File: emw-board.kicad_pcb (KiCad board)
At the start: 2 copper layers, 49.5 x 48.3 mm, 36 parts, among them P1 1WIRE, P2 BATT, P3 CONN_01X06, P4 SWDN, P5 CONS, P6 OLED, P7 CONN_01X07, SW1 B3S-1000, SW2 B3S-1000, U1 MAX604CSA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

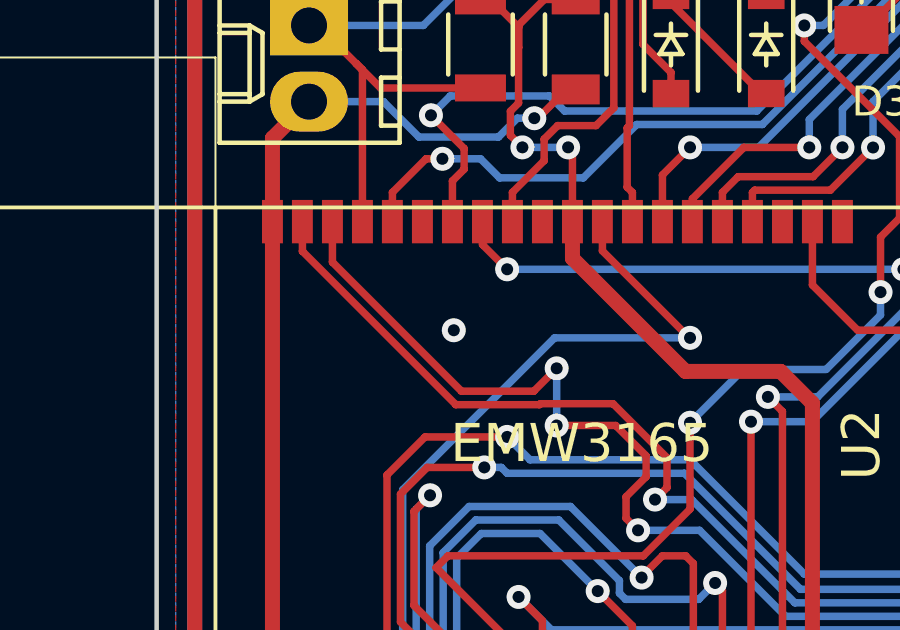
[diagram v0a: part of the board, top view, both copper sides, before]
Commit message: Regenerate copper pours.
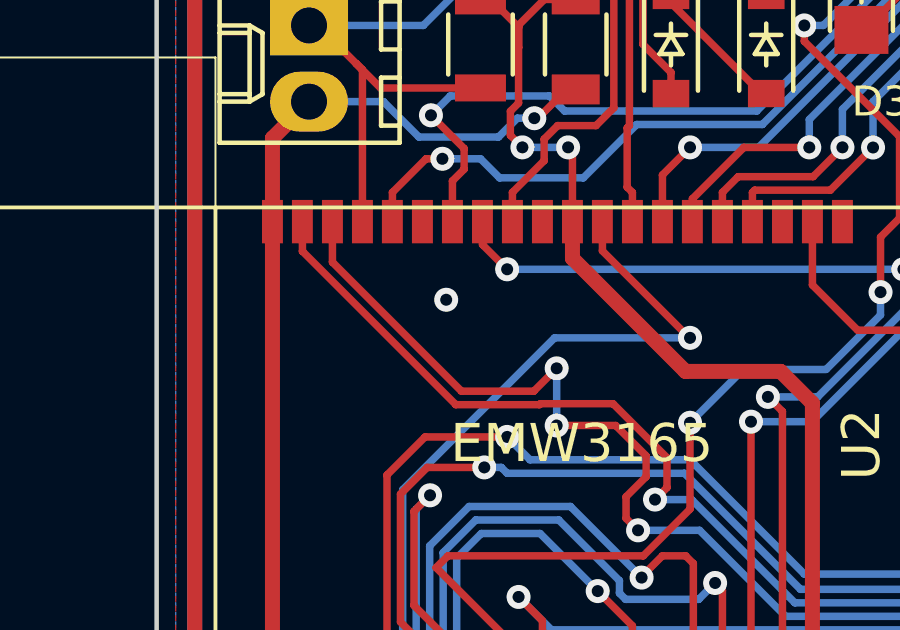
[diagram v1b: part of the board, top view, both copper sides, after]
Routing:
- net GND: vias 7 -> 8
- net (no net): vias 1 -> 0
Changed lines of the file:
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@@
     (visible_elements 7FFEFF7F)
     (pcbplotparams
-      (layerselection 0x010f0_ffffffff)
+      (layerselection 0x010f0_80000001)
       (usegerberextensions true)
       (excludeedgelayer true)
@@
   (gr_line (start 163.83 53.34) (end 163.83 101.6) (layer Edge.Cuts) (width 0.15))
   (gr_line (start 114.3 53.34) (end 163.83 53.34) (layer Edge.Cuts) (width 0.15))
-  (via (at 124.206 72.39) (size 0.8) (drill 0.4) (layers F.Cu B.Cu) (net 0))
   (segment (start 119.38 62.23) (end 123.19 62.23) (width 0.25) (layer B.Cu) (net 1) (status 10))
   (segment (start 123.19 62.23) (end 125.73 59.69) (width 0.25) (layer B.Cu) (net 1))
@@
   (segment (start 123.31841 76.962) (end 125.222 76.962) (width 0.25) (layer F.Cu) (net 4))
   (via (at 125.222 76.962) (size 0.8) (drill 0.4) (layers F.Cu B.Cu) (net 4))
+  (via (at 123.952 71.374) (size 0.8) (drill 0.4) (layers F.Cu B.Cu) (net 8))
   (segment (start 159.512 88.392) (end 159.512 89.892) (width 0.5) (layer F.Cu) (net 8) (status 10))
   (segment (start 159.512 89.892) (end 157.48 91.924) (width 0.5) (layer F.Cu) (net 8))

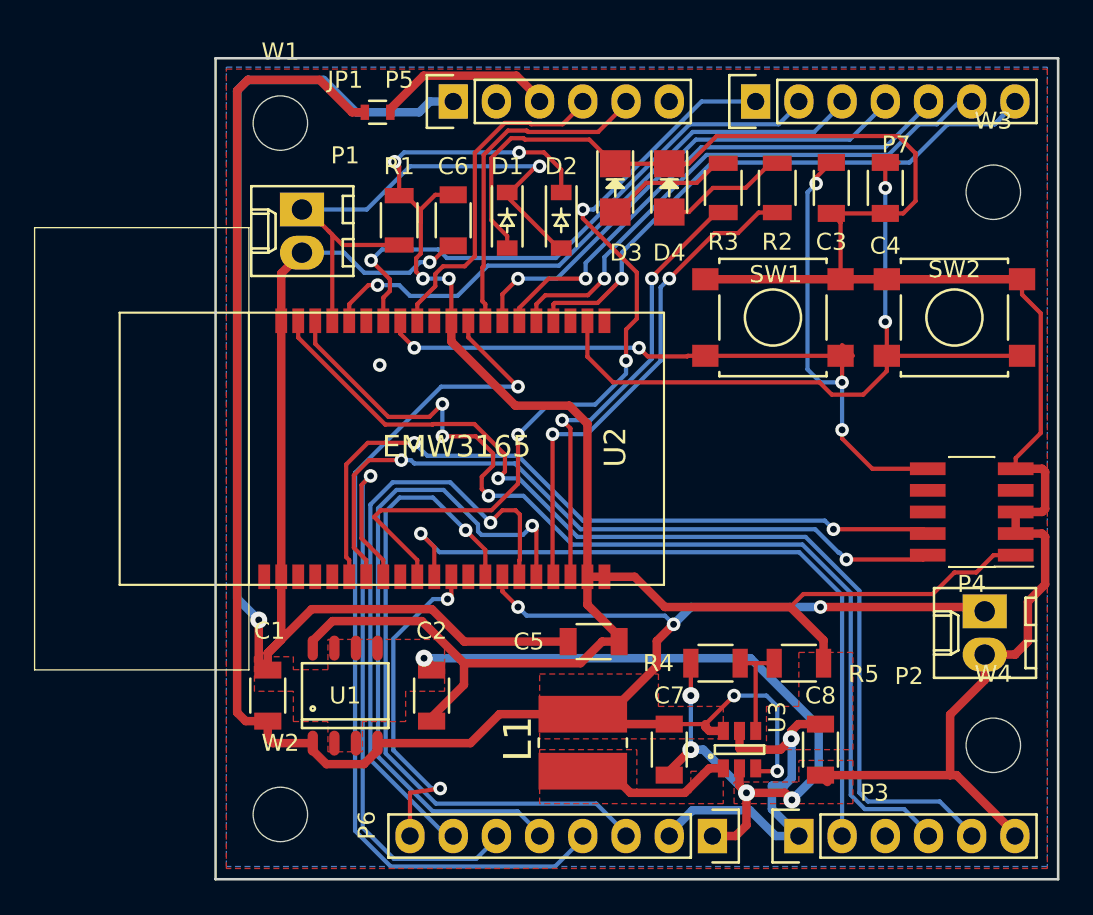
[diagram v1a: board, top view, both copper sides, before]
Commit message: Move power and 1-wire connector so that right-angled type can also be used.
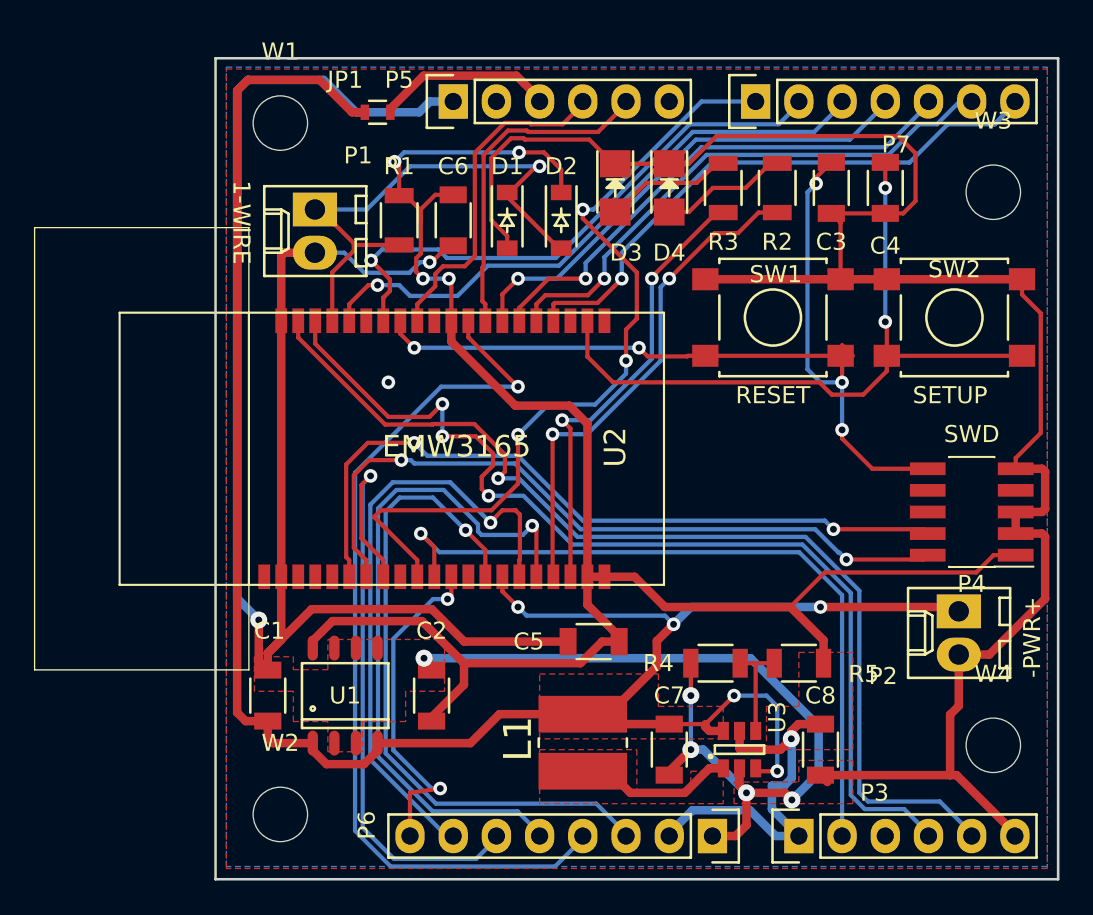
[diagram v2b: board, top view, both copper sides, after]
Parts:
- moved P2 1.52 mm to (158.0, 85.9)
- moved P1 0.76 mm to (120.1, 62.2)
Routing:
- net +BATT: track 127.6 -> 125.5 mm
- net Net-(D1-Pad1): track 34.2 -> 33.1 mm
- net GND: track 270.9 -> 271.5 mm
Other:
- board text added: "-PWR+"
- board text added: "1-WIRE"
- board text added: "RESET"
- board text added: "SETUP"

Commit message: Rotate 1-wire connector.
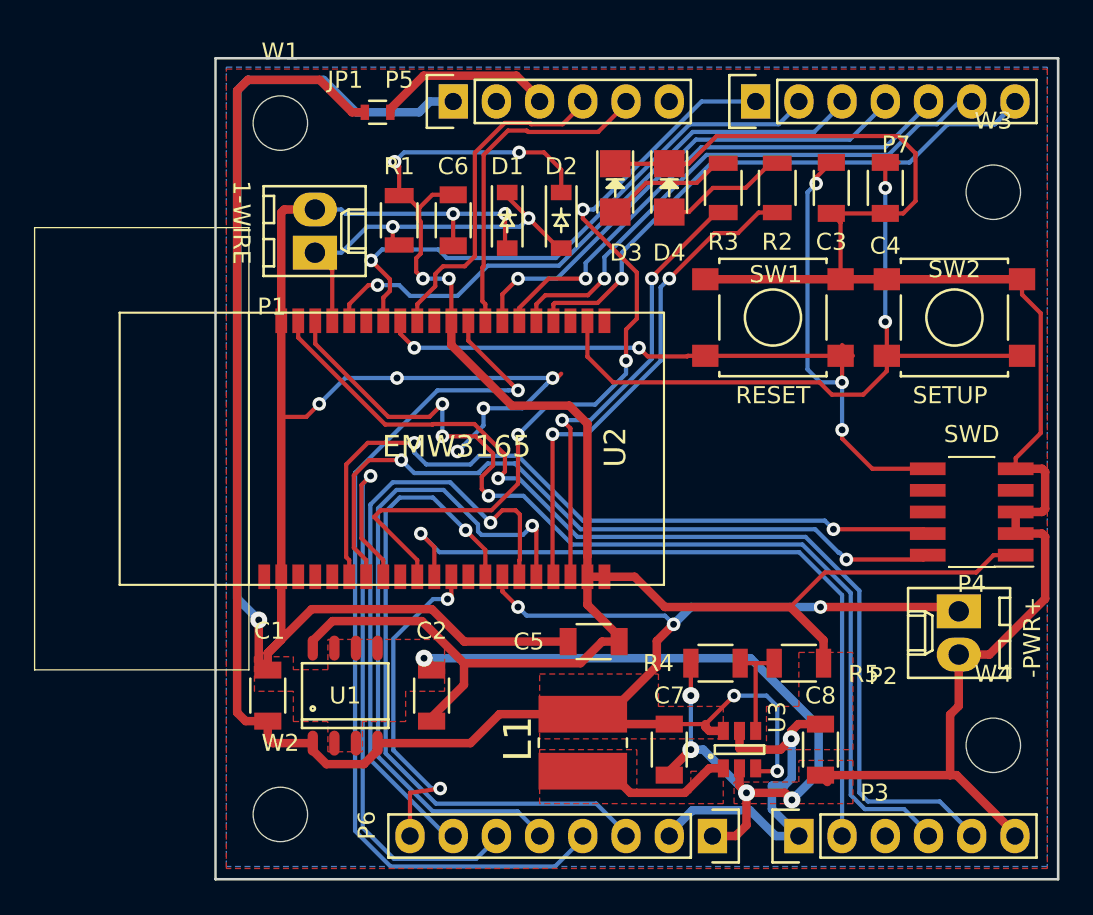
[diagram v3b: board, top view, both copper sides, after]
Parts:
- moved P1 2.54 mm to (120.1, 64.8), turned to 90 degrees
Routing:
- net GND: track 271.5 -> 291.8 mm, vias 8 -> 13
- net Net-(D1-Pad1): track 33.1 -> 24.2 mm, vias 1 -> 2
- net Net-(P4-Pad4): track 43.6 -> 44.4 mm
- net Net-(P4-Pad2): track 42.9 -> 43.4 mm

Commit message: Fix swd connector placing.
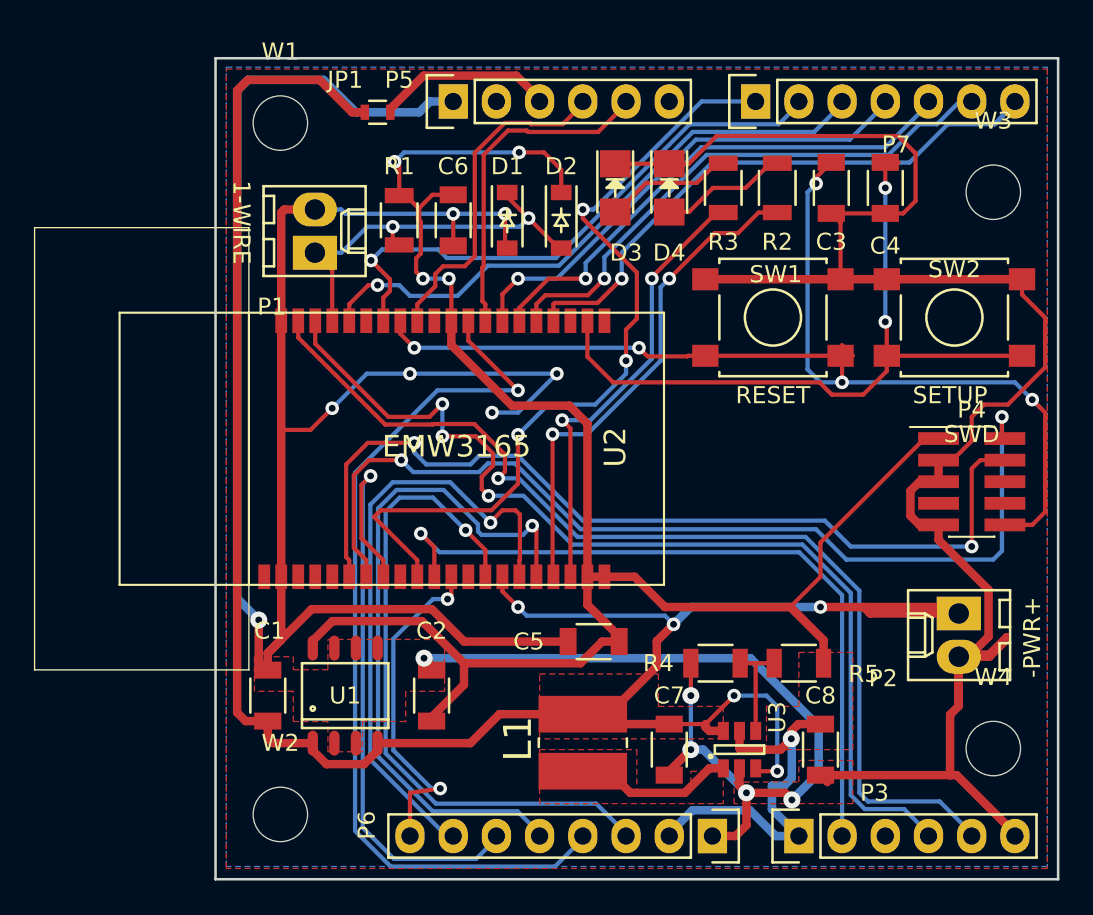
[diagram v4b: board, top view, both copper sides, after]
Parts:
- P4: footprint Pin_Headers:Pin_Header_Straight_2x05_Pitch1.27mm_SMD -> stonepile:swd_connector_2x05_Pitch1.27mm_SMD
- moved P4 1.78 mm to (158.8, 78.2), turned to 0 degrees
- moved W4 0.19 mm to (160.0, 93.9)
- moved P2 0.13 mm to (158.0, 86.0)
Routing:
- net Net-(P4-Pad2): track 43.4 -> 57.0 mm
- net Net-(C3-Pad1): track 54.6 -> 68.1 mm
- net Net-(P4-Pad4): track 44.4 -> 54.0 mm
- net GND: track 291.8 -> 298.6 mm, vias 13 -> 12
- net +BATT: track 125.5 -> 131.3 mm
- net +3V3: track 131.3 -> 130.7 mm

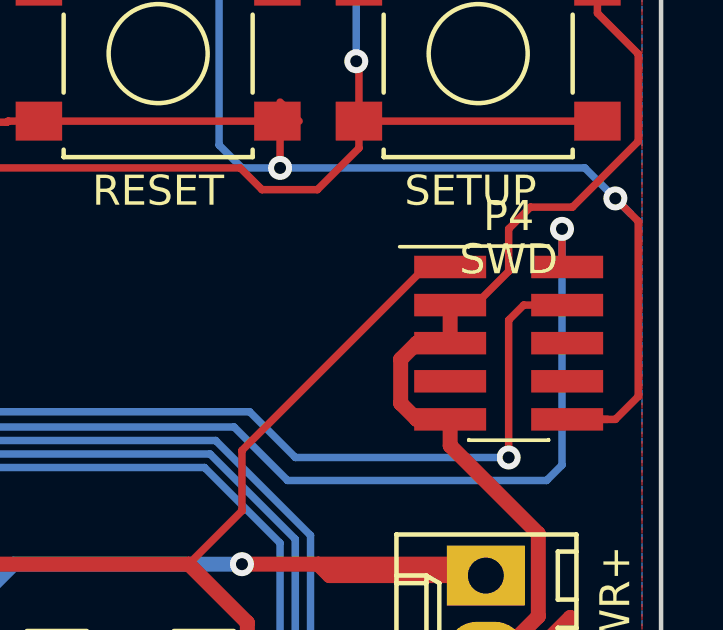
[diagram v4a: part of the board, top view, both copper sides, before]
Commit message: Add BOM info.
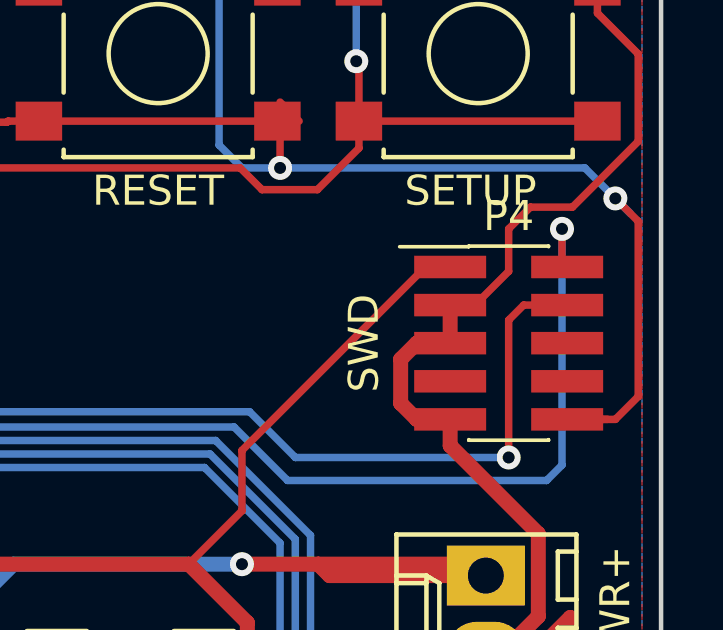
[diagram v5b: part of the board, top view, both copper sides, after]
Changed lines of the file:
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@@
     (links 93)
     (no_connects 0)
-    (area 114.224999 53.264999 163.905001 101.675001)
+    (area 103.429459 50.846666 163.905001 104.093333)
     (thickness 1.6)
     (drawings 38)
@@
     (effects (font (size 1.5 1.5) (thickness 0.3)) (justify mirror))
   )
-  (gr_text SWD (at 158.75 75.438) (layer F.SilkS)
+  (gr_text SWD (at 153.924 78.232 90) (layer F.SilkS)
     (effects (font (size 1 1) (thickness 0.25)))
   )

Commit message: Cleanup some tracks.
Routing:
- net GND: track 298.6 -> 292.0 mm
- net +BATT: track 131.3 -> 125.9 mm
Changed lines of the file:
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@@
     (thickness 1.6)
     (drawings 38)
-    (tracks 631)
+    (tracks 625)
     (zones 0)
     (modules 36)
@@
   )
   (setup
-    (last_trace_width 0.25)
+    (last_trace_width 0.5)
     (user_trace_width 0.25)
     (user_trace_width 0.5)
@@
   (segment (start 123.31841 76.962) (end 125.222 76.962) (width 0.25) (layer F.Cu) (net 4))
   (via (at 125.222 76.962) (size 0.8) (drill 0.4) (layers F.Cu B.Cu) (net 4))
+  (segment (start 157.988 88.519) (end 158.558002 88.519) (width 0.5) (layer F.Cu) (net 8))
+  (segment (start 158.558002 88.519) (end 159.738001 87.339001) (width 0.5) (layer F.Cu) (net 8))
+  (segment (start 159.738001 87.339001) (end 159.738001 84.585001) (width 0.5) (layer F.Cu) (net 8))
+  (segment (start 159.738001 84.585001) (end 156.8 81.647) (width 0.5) (layer F.Cu) (net 8))
   (segment (start 132.08 74.168) (end 130.556 74.168) (width 0.25) (layer B.Cu) (net 8))
   (via (at 130.556 74.168) (size 0.8) (drill 0.4) (layers F.Cu B.Cu) (net 8))
@@
   (segment (start 155.149999 78.766999) (end 155.684998 78.232) (width 0.5) (layer F.Cu) (net 8) (status 20))
   (segment (start 155.684998 78.232) (end 156.8 78.232) (width 0.5) (layer F.Cu) (net 8) (status 30))
-  (segment (start 157.988 88.519) (end 158.558002 88.519) (width 0.5) (layer F.Cu) (net 8) (status 30))
-  (segment (start 158.558002 88.519) (end 159.738001 87.339001) (width 0.5) (layer F.Cu) (net 8) (status 10))
-  (segment (start 159.738001 84.585001) (end 156.8 81.647) (width 0.5) (layer F.Cu) (net 8))
-  (segment (start 159.738001 87.339001) (end 159.738001 84.585001) (width 0.5) (layer F.Cu) (net 8))
   (segment (start 156.8 81.647) (end 156.8 80.772) (width 0.5) (layer F.Cu) (net 8) (status 20))
-  (segment (start 160.804 87.376) (end 159.788 88.392) (width 0.5) (layer F.Cu) (net 8))
-  (segment (start 160.804 87.376) (end 160.804 87.503) (width 0.5) (layer F.Cu) (net 8))
-  (segment (start 160.804 87.503) (end 159.788 88.519) (width 0.5) (layer F.Cu) (net 8))
-  (segment (start 159.788 88.519) (end 157.988 88.519) (width 0.5) (layer F.Cu) (net 8) (status 20))
   (segment (start 157.48 91.924) (end 157.988 91.416) (width 0.5) (layer F.Cu) (net 8))
   (segment (start 157.988 91.416) (end 157.988 88.519) (width 0.5) (layer F.Cu) (net 8) (status 20))
@@
   (segment (start 118.342 62.23) (end 120.142 62.23) (width 0.5) (layer F.Cu) (net 8) (status 20))
   (segment (start 120.142 62.23) (end 120.442 62.23) (width 0.25) (layer F.Cu) (net 8) (status 30))
-  (segment (start 159.788 88.392) (end 157.988 88.392) (width 0.5) (layer F.Cu) (net 8) (status 20))
   (segment (start 157.988 91.416) (end 157.988 88.392) (width 0.5) (layer F.Cu) (net 8) (status 20))
   (segment (start 157.48 91.924) (end 157.48 95.48) (width 0.5) (layer F.Cu) (net 8))
@@
   (segment (start 146.05 88.9) (end 147.14 88.9) (width 0.25) (layer F.Cu) (net 44) (status 20))
   (segment (start 146.05 92.88) (end 146.05 88.9) (width 0.25) (layer F.Cu) (net 44) (status 10))
-  (segment (start 152.4 85.598) (end 157.734 85.598) (width 0.5) (layer F.Cu) (net 45) (status 20))
   (segment (start 152.781 85.979) (end 157.988 85.979) (width 0.5) (layer F.Cu) (net 45) (status 20))
   (segment (start 149.86 85.598) (end 152.4 85.598) (width 0.5) (layer F.Cu) (net 45))

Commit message: Remove old silkscreen text for unconnected pin.
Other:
- board text removed: "PB8"
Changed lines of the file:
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@@
     (area 103.429459 50.846666 163.905001 104.093333)
     (thickness 1.6)
-    (drawings 38)
+    (drawings 37)
     (tracks 625)
     (zones 0)
@@
   )
   (setup
-    (last_trace_width 0.5)
+    (last_trace_width 0.25)
     (user_trace_width 0.25)
     (user_trace_width 0.5)
@@
     (effects (font (size 1 1) (thickness 0.15)) (justify right mirror))
   )
-  (gr_text PB8 (at 153.67 97.79 90) (layer B.SilkS)
-    (effects (font (size 1 1) (thickness 0.15)) (justify right mirror))
-  )
